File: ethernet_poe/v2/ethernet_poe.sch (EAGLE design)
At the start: 86 parts, among them J3 ARJM11C7-104-AB-EW2, Q1 BSR16, U1 AZ1117EH-3.3TRG1, U2 IFX91041, U3 W5500, U4 TPS26600PWPR, X1 25MHz

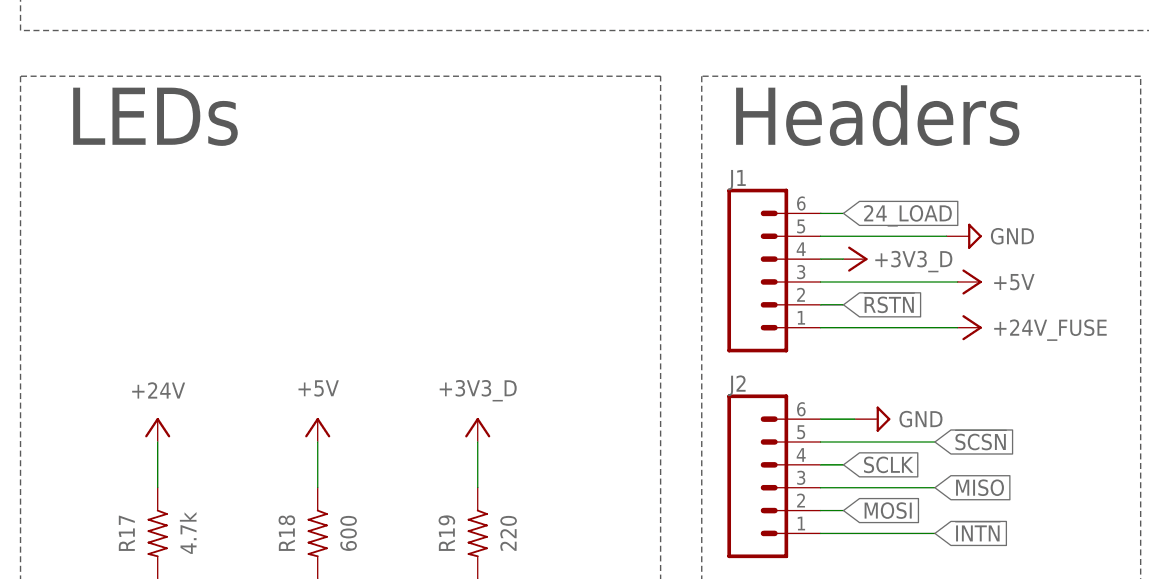
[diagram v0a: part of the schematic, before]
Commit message: routing for efuse
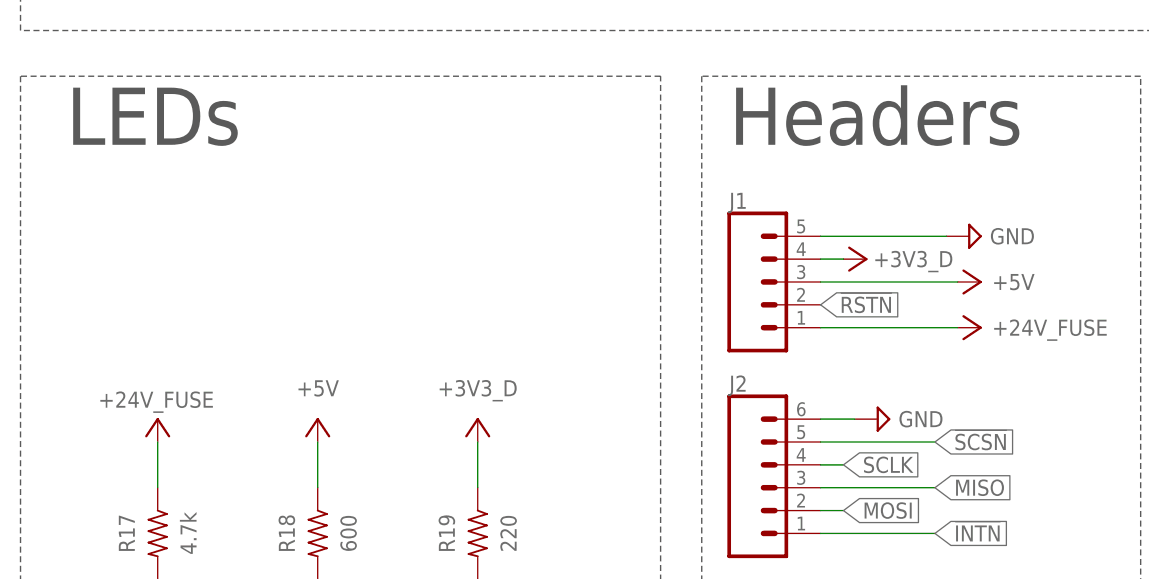
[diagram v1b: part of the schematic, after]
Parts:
- J1: device SparkFun-Connectors:CONN_06SILK_FEMALE_PTH -> SparkFun-Connectors:CONN_05
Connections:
- net +24V: no longer R17.1
- net +24V_FUSE: now also R17.1
- net 24_LOAD: no longer J1.6
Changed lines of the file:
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@@
 <?xml version="1.0" encoding="utf-8"?>
 <!DOCTYPE eagle SYSTEM "eagle.dtd">
-<eagle version="9.6.0">
+<eagle version="9.5.2">
 <drawing>
 <settings>
@@
 <part name="SUPPLY7" library="supply2" library_urn="urn:adsk.eagle:library:372" deviceset="GND" device=""/>
 <part name="C15" library="rcl" library_urn="urn:adsk.eagle:library:334" deviceset="CPOL-US" device="E2-5" package3d_urn="urn:adsk.eagle:package:23346/2" value="100uF"/>
-<part name="J1" library="SparkFun-Connectors" library_urn="urn:adsk.eagle:library:513" deviceset="CONN_06" device="SILK_FEMALE_PTH" package3d_urn="urn:adsk.eagle:package:38009/1"/>
+<part name="J1" library="SparkFun-Connectors" deviceset="CONN_05" device="" package3d_urn="urn:adsk.eagle:package:38104/1"/>
 <part name="J2" library="SparkFun-Connectors" library_urn="urn:adsk.eagle:library:513" deviceset="CONN_06" device="SILK_FEMALE_PTH" package3d_urn="urn:adsk.eagle:package:38009/1"/>
 <part name="SUPPLY12" library="supply2" library_urn="urn:adsk.eagle:library:372" deviceset="GND" device=""/>
@@
 <part name="+24V_FUSE2" library="ethernet_poe" deviceset="+24V_FUSE" device=""/>
 <part name="R30" library="rcl" library_urn="urn:adsk.eagle:library:334" deviceset="R-US_" device="R0603" package3d_urn="urn:adsk.eagle:package:23555/3" value="715k"/>
-<part name="+24V3" library="ethernet_poe" deviceset="+24V" device=""/>
 <part name="R31" library="rcl" library_urn="urn:adsk.eagle:library:334" deviceset="R-US_" device="R0603" package3d_urn="urn:adsk.eagle:package:23555/3" value="20k"/>
 <part name="R32" library="rcl" library_urn="urn:adsk.eagle:library:334" deviceset="R-US_" device="R0603" package3d_urn="urn:adsk.eagle:package:23555/3" value="30.1k"/>
@@
 <part name="SUPPLY30" library="supply2" library_urn="urn:adsk.eagle:library:372" deviceset="GND" device=""/>
 <part name="+24V_FUSE3" library="ethernet_poe" deviceset="+24V_FUSE" device=""/>
+<part name="+24V_FUSE4" library="ethernet_poe" deviceset="+24V_FUSE" device=""/>
 </parts>
 <sheets>
@@
 <attribute name="VALUE" x="313.436" y="216.789" size="1.778" layer="96"/>
 </instance>
-<instance part="J1" gate="G$1" x="91.44" y="119.38" smashed="yes">
-<attribute name="VALUE" x="88.9" y="109.474" size="1.778" layer="96" font="vector"/>
-<attribute name="NAME" x="86.36" y="130.048" size="1.778" layer="95"/>
+<instance part="J1" gate="G$1" x="88.9" y="119.38" smashed="yes">
+<attribute name="VALUE" x="86.36" y="109.474" size="1.778" layer="96" font="vector"/>
+<attribute name="NAME" x="86.36" y="127.508" size="1.778" layer="95"/>
 </instance>
 <instance part="J2" gate="G$1" x="91.44" y="96.52" smashed="yes">
@@
 <attribute name="VALUE" x="328.93" y="109.22" size="1.778" layer="96"/>
 </instance>
-<instance part="+24V3" gate="G$1" x="22.86" y="104.14" smashed="yes">
-<attribute name="VALUE" x="22.86" y="106.426" size="1.778" layer="96" align="bottom-center"/>
-</instance>
 <instance part="R31" gate="G$1" x="327.66" y="96.52" smashed="yes" rot="R270">
 <attribute name="NAME" x="328.93" y="96.52" size="1.778" layer="95"/>
@@
 <instance part="+24V_FUSE3" gate="G$1" x="218.44" y="254" smashed="yes">
 <attribute name="VALUE" x="211.836" y="255.27" size="1.778" layer="96"/>
+</instance>
+<instance part="+24V_FUSE4" gate="G$1" x="22.86" y="104.14" smashed="yes">
+<attribute name="VALUE" x="16.256" y="105.41" size="1.778" layer="96"/>
 </instance>
 </instances>
@@
 <segment>
 <pinref part="+3V3_D9" gate="G$1" pin="+3V3_D"/>
-<wire x1="99.06" y1="121.92" x2="96.52" y2="121.92" width="0.1524" layer="91"/>
 <pinref part="J1" gate="G$1" pin="4"/>
+<wire x1="96.52" y1="121.92" x2="99.06" y2="121.92" width="0.1524" layer="91"/>
 </segment>
 <segment>
@@
 </segment>
 <segment>
-<pinref part="R17" gate="G$1" pin="1"/>
-<wire x1="22.86" y1="96.52" x2="22.86" y2="101.6" width="0.1524" layer="91"/>
-<pinref part="+24V3" gate="G$1" pin="+24V"/>
-</segment>
-<segment>
 <pinref part="U4" gate="A" pin="!SHDN"/>
 <wire x1="393.7" y1="104.14" x2="406.4" y2="104.14" width="0.1524" layer="91"/>
@@
 </segment>
 <segment>
-<label x="99.06" y="116.84" size="1.778" layer="95" xref="yes"/>
-<wire x1="96.52" y1="116.84" x2="99.06" y2="116.84" width="0.1524" layer="91"/>
+<label x="96.52" y="116.84" size="1.778" layer="95" xref="yes"/>
 <pinref part="J1" gate="G$1" pin="2"/>
 </segment>
@@
 <pinref part="+24V_FUSE3" gate="G$1" pin="+24V_FUSE"/>
 </segment>
+<segment>
+<pinref part="R17" gate="G$1" pin="1"/>
+<wire x1="22.86" y1="96.52" x2="22.86" y2="101.6" width="0.1524" layer="91"/>
+<pinref part="+24V_FUSE4" gate="G$1" pin="+24V_FUSE"/>
+</segment>
 </net>
 <net name="N$9" class="0">
@@
 </segment>
 </net>
-<net name="N$33" class="0">
+<net name="N$33" class="1">
 <segment>
 <pinref part="U4" gate="A" pin="ILIM"/>
@@
 <label x="408.94" y="99.06" size="1.778" layer="95" xref="yes"/>
 </segment>
-<segment>
-<pinref part="J1" gate="G$1" pin="6"/>
-<wire x1="96.52" y1="127" x2="99.06" y2="127" width="0.1524" layer="91"/>
-<label x="99.06" y="127" size="1.778" layer="95" xref="yes"/>
-</segment>
-</net>
+</net>

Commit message: Pre Review Commit, Completed Routing
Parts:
- added H1, H2: MOUNT-PAD-ROUND2.8, holes:MOUNT-PAD-ROUND2.8
- J2: device SparkFun-Connectors:CONN_06SILK_FEMALE_PTH -> SparkFun-Connectors:CONN_07
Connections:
- net 24_LOAD: now also J2.7
- net GND: now also H1.MOUNT, H2.MOUNT
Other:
- note removed: "Add pi filter"
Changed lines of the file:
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@@
 <part name="C15" library="rcl" library_urn="urn:adsk.eagle:library:334" deviceset="CPOL-US" device="E2-5" package3d_urn="urn:adsk.eagle:package:23346/2" value="100uF"/>
 <part name="J1" library="SparkFun-Connectors" deviceset="CONN_05" device="" package3d_urn="urn:adsk.eagle:package:38104/1"/>
-<part name="J2" library="SparkFun-Connectors" library_urn="urn:adsk.eagle:library:513" deviceset="CONN_06" device="SILK_FEMALE_PTH" package3d_urn="urn:adsk.eagle:package:38009/1"/>
+<part name="J2" library="SparkFun-Connectors" library_urn="urn:adsk.eagle:library:513" deviceset="CONN_07" device="" package3d_urn="urn:adsk.eagle:package:38129/1"/>
 <part name="SUPPLY12" library="supply2" library_urn="urn:adsk.eagle:library:372" deviceset="GND" device=""/>
 <part name="P+7" library="supply1" library_urn="urn:adsk.eagle:library:371" deviceset="+5V" device=""/>
@@
 <part name="+24V_FUSE3" library="ethernet_poe" deviceset="+24V_FUSE" device=""/>
 <part name="+24V_FUSE4" library="ethernet_poe" deviceset="+24V_FUSE" device=""/>
+<part name="SUPPLY31" library="supply2" library_urn="urn:adsk.eagle:library:372" deviceset="GND" device=""/>
+<part name="H1" library="holes" library_urn="urn:adsk.eagle:library:237" deviceset="MOUNT-PAD-ROUND" device="2.8" package3d_urn="urn:adsk.eagle:package:14281/1"/>
+<part name="H2" library="holes" library_urn="urn:adsk.eagle:library:237" deviceset="MOUNT-PAD-ROUND" device="2.8" package3d_urn="urn:adsk.eagle:package:14281/1"/>
+<part name="SUPPLY32" library="supply2" library_urn="urn:adsk.eagle:library:372" deviceset="GND" device=""/>
 </parts>
 <sheets>
@@
 blown-fuse-indicator-circuit-
 using-one-transistor/</text>
-<text x="223.52" y="241.3" size="1.778" layer="91">Add pi filter</text>
 <text x="335.28" y="157.48" size="1.778" layer="97">NOTE: This pi filter isolates the digital
 and analog 3.3V power supplies by
@@
 <attribute name="NAME" x="86.36" y="127.508" size="1.778" layer="95"/>
 </instance>
-<instance part="J2" gate="G$1" x="91.44" y="96.52" smashed="yes">
-<attribute name="VALUE" x="88.9" y="86.614" size="1.778" layer="96" font="vector"/>
-<attribute name="NAME" x="86.36" y="107.188" size="1.778" layer="95"/>
+<instance part="J2" gate="G$1" x="91.44" y="91.44" smashed="yes">
+<attribute name="VALUE" x="88.9" y="81.534" size="1.778" layer="96" font="vector"/>
+<attribute name="NAME" x="86.36" y="104.648" size="1.778" layer="95"/>
 </instance>
 <instance part="SUPPLY12" gate="GND" x="113.03" y="124.46" smashed="yes" rot="R90">
@@
 <attribute name="VALUE" x="415.036" y="112.649" size="1.778" layer="96"/>
 </instance>
-<instance part="SUPPLY30" gate="GND" x="102.87" y="104.14" smashed="yes" rot="R90">
-<attribute name="VALUE" x="105.156" y="104.14" size="1.778" layer="96" align="center-left"/>
+<instance part="SUPPLY30" gate="GND" x="102.87" y="99.06" smashed="yes" rot="R90">
+<attribute name="VALUE" x="105.156" y="99.06" size="1.778" layer="96" align="center-left"/>
 </instance>
 <instance part="+24V_FUSE3" gate="G$1" x="218.44" y="254" smashed="yes">
@@
 <instance part="+24V_FUSE4" gate="G$1" x="22.86" y="104.14" smashed="yes">
 <attribute name="VALUE" x="16.256" y="105.41" size="1.778" layer="96"/>
+</instance>
+<instance part="SUPPLY31" gate="GND" x="40.64" y="7.62" smashed="yes">
+<attribute name="VALUE" x="40.64" y="5.588" size="1.778" layer="96" align="top-center"/>
+</instance>
+<instance part="H1" gate="G$1" x="48.26" y="12.7" smashed="yes">
+<attribute name="NAME" x="51.054" y="13.2842" size="1.778" layer="95"/>
+<attribute name="VALUE" x="42.418" y="7.9502" size="1.778" layer="96"/>
+</instance>
+<instance part="H2" gate="G$1" x="81.28" y="12.7" smashed="yes">
+<attribute name="NAME" x="84.074" y="13.2842" size="1.778" layer="95"/>
+<attribute name="VALUE" x="75.946" y="7.9502" size="1.778" layer="96"/>
+</instance>
+<instance part="SUPPLY32" gate="GND" x="73.66" y="7.62" smashed="yes">
+<attribute name="VALUE" x="73.66" y="5.588" size="1.778" layer="96" align="top-center"/>
 </instance>
 </instances>
@@
 <segment>
 <pinref part="J2" gate="G$1" pin="6"/>
-<wire x1="96.52" y1="104.14" x2="100.33" y2="104.14" width="0.1524" layer="91"/>
+<wire x1="96.52" y1="99.06" x2="100.33" y2="99.06" width="0.1524" layer="91"/>
 <pinref part="SUPPLY30" gate="GND" pin="GND"/>
+</segment>
+<segment>
+<pinref part="SUPPLY31" gate="GND" pin="GND"/>
+<wire x1="40.64" y1="10.16" x2="40.64" y2="12.7" width="0.1524" layer="91"/>
+<pinref part="H1" gate="G$1" pin="MOUNT"/>
+<wire x1="40.64" y1="12.7" x2="45.72" y2="12.7" width="0.1524" layer="91"/>
+</segment>
+<segment>
+<pinref part="SUPPLY32" gate="GND" pin="GND"/>
+<wire x1="73.66" y1="10.16" x2="73.66" y2="12.7" width="0.1524" layer="91"/>
+<pinref part="H2" gate="G$1" pin="MOUNT"/>
+<wire x1="73.66" y1="12.7" x2="78.74" y2="12.7" width="0.1524" layer="91"/>
 </segment>
 </net>
@@
 </segment>
 <segment>
-<label x="109.22" y="101.6" size="1.778" layer="95" xref="yes"/>
-<wire x1="96.52" y1="101.6" x2="109.22" y2="101.6" width="0.1524" layer="91"/>
+<label x="109.22" y="96.52" size="1.778" layer="95" xref="yes"/>
+<wire x1="96.52" y1="96.52" x2="109.22" y2="96.52" width="0.1524" layer="91"/>
 <pinref part="J2" gate="G$1" pin="5"/>
 </segment>
@@
 </segment>
 <segment>
-<wire x1="96.52" y1="99.06" x2="99.06" y2="99.06" width="0.1524" layer="91"/>
-<label x="99.06" y="99.06" size="1.778" layer="95" xref="yes"/>
+<wire x1="96.52" y1="93.98" x2="99.06" y2="93.98" width="0.1524" layer="91"/>
+<label x="99.06" y="93.98" size="1.778" layer="95" xref="yes"/>
 <pinref part="J2" gate="G$1" pin="4"/>
 </segment>
@@
 </segment>
 <segment>
-<wire x1="96.52" y1="96.52" x2="109.22" y2="96.52" width="0.1524" layer="91"/>
-<label x="109.22" y="96.52" size="1.778" layer="95" xref="yes"/>
+<wire x1="96.52" y1="91.44" x2="109.22" y2="91.44" width="0.1524" layer="91"/>
+<label x="109.22" y="91.44" size="1.778" layer="95" xref="yes"/>
 <pinref part="J2" gate="G$1" pin="3"/>
 </segment>
@@
 </segment>
 <segment>
-<wire x1="96.52" y1="93.98" x2="99.06" y2="93.98" width="0.1524" layer="91"/>
-<label x="99.06" y="93.98" size="1.778" layer="95" xref="yes"/>
+<wire x1="96.52" y1="88.9" x2="99.06" y2="88.9" width="0.1524" layer="91"/>
+<label x="99.06" y="88.9" size="1.778" layer="95" xref="yes"/>
 <pinref part="J2" gate="G$1" pin="2"/>
 </segment>
@@
 </segment>
 <segment>
-<label x="109.22" y="91.44" size="1.778" layer="95" xref="yes"/>
-<wire x1="96.52" y1="91.44" x2="109.22" y2="91.44" width="0.1524" layer="91"/>
+<label x="109.22" y="86.36" size="1.778" layer="95" xref="yes"/>
+<wire x1="96.52" y1="86.36" x2="109.22" y2="86.36" width="0.1524" layer="91"/>
 <pinref part="J2" gate="G$1" pin="1"/>
 </segment>
@@
 </segment>
 <segment>
-<label x="96.52" y="116.84" size="1.778" layer="95" xref="yes"/>
+<label x="101.6" y="116.84" size="1.778" layer="95" xref="yes"/>
 <pinref part="J1" gate="G$1" pin="2"/>
+<wire x1="96.52" y1="116.84" x2="101.6" y2="116.84" width="0.1524" layer="91"/>
 </segment>
 <segment>
@@
 <label x="408.94" y="99.06" size="1.778" layer="95" xref="yes"/>
 </segment>
-</net>
+<segment>
+<pinref part="J2" gate="G$1" pin="7"/>
+<wire x1="96.52" y1="101.6" x2="109.22" y2="101.6" width="0.1524" layer="91"/>
+<label x="109.22" y="101.6" size="1.778" layer="95" xref="yes"/>
+</segment>
+</net>

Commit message: Additional design review updates
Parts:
- C1: value 22nF -> 22nF, 50V
- C27, C28: value (none) -> TBD
- C3: value 2.2uF -> 2.2uF, 50V
- C30: value 1uF -> 1uF, 50V
- C31: value 2.2mF -> 2.2mF, 50V
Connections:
- new net !RST: C17.1, R20.1, S1.2
- net !RSTN: no longer C17.1, R20.1, S1.2
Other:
- note added: "3.3V Analog"
- note added: "Filtering"
- note added: "GND Analog"
- note added: "Mounting Holes"
- note added: "NOTE: This pi filter isolates the digital and analog 3.3V power supplies by attenuating differential mode noise. Cap values TBD based on noise."
- note added: "Power (24V-5V)"
- note added: "Power (5V-3.3V)"
- note removed: "3.3V Analog Filtering"
- note removed: "NOTE: This pi filter isolates the digital and analog 3.3V power supplies by attenuating differential mode noise."
- note removed: "Power"
- moved on the sheet: C1, C10, C11, C12, C13, C14, C15, C16, C17, C18, C19, C2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

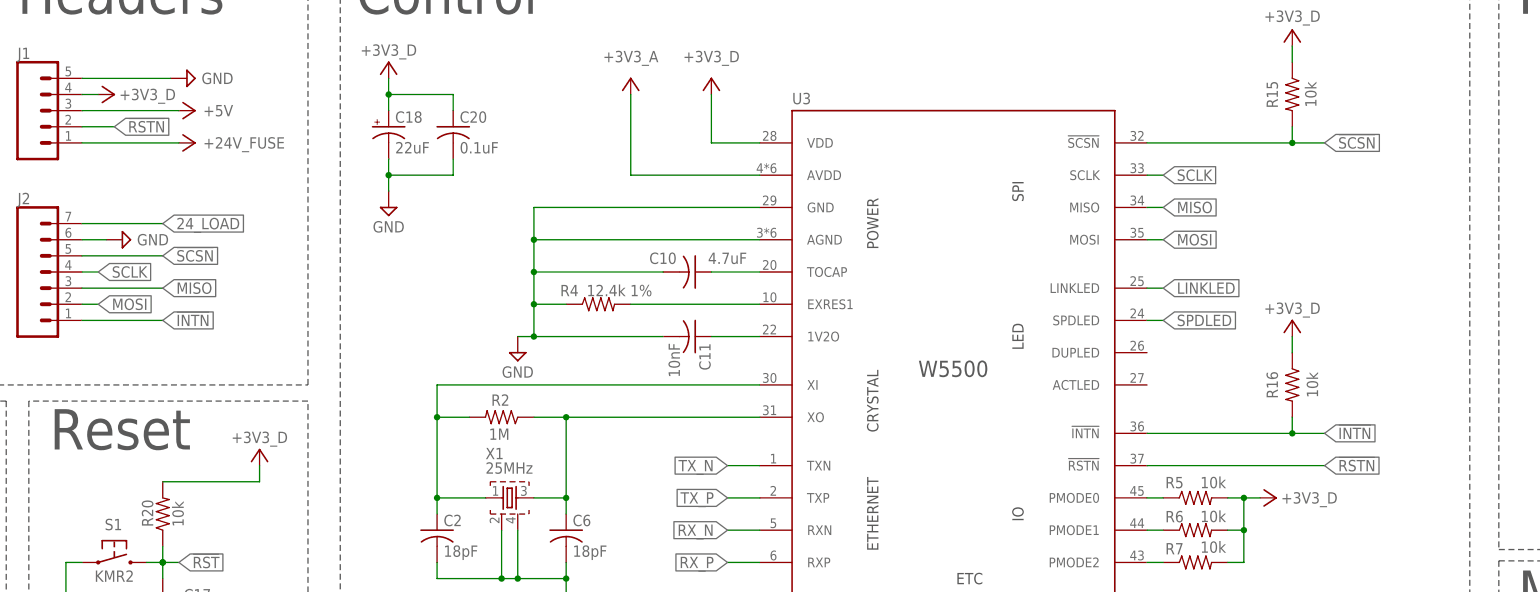
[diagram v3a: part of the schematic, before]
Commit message: Made drc compliant
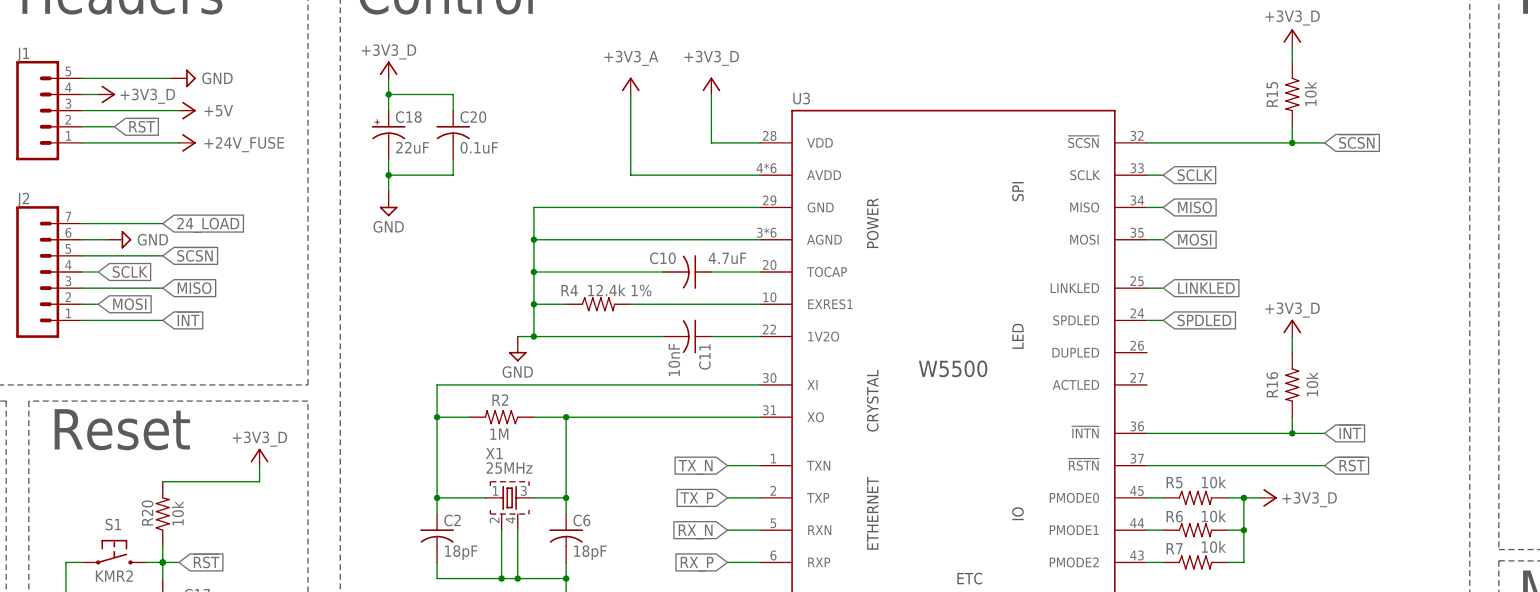
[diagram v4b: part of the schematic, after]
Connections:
- net !INTN renamed !INT
- removed net !RSTN: J1.2, U3.!RSTN
- net !RST: now also J1.2, U3.!RSTN
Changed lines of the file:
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@@
-</segment>
-</net>
-<net name="!INTN" class="0">
-<segment>
-<pinref part="U3" gate="G$1" pin="!INTN"/>
-<wire x1="264.16" y1="96.52" x2="287.02" y2="96.52" width="0.1524" layer="91"/>
-<label x="292.1" y="96.52" size="1.778" layer="95" xref="yes"/>
-<pinref part="R16" gate="G$1" pin="2"/>
-<wire x1="287.02" y1="96.52" x2="292.1" y2="96.52" width="0.1524" layer="91"/>
-<wire x1="287.02" y1="99.06" x2="287.02" y2="96.52" width="0.1524" layer="91"/>
-<junction x="287.02" y="96.52"/>
-</segment>
-<segment>
-<label x="109.22" y="114.3" size="1.778" layer="95" xref="yes"/>
-<wire x1="96.52" y1="114.3" x2="109.22" y2="114.3" width="0.1524" layer="91"/>
-<pinref part="J2" gate="G$1" pin="1"/>
-</segment>
-</net>
-<net name="!RSTN" class="0">
-<segment>
-<pinref part="U3" gate="G$1" pin="!RSTN"/>
-<wire x1="264.16" y1="91.44" x2="292.1" y2="91.44" width="0.1524" layer="91"/>
-<label x="292.1" y="91.44" size="1.778" layer="95" xref="yes"/>
-</segment>
-<segment>
-<label x="101.6" y="144.78" size="1.778" layer="95" xref="yes"/>
-<pinref part="J1" gate="G$1" pin="2"/>
-<wire x1="96.52" y1="144.78" x2="101.6" y2="144.78" width="0.1524" layer="91"/>
 </segment>
 </net>
@@
 <wire x1="109.22" y1="76.2" x2="109.22" y2="78.74" width="0.1524" layer="91"/>
 </segment>
-</net>
+<segment>
+<pinref part="U3" gate="G$1" pin="!RSTN"/>
+<wire x1="264.16" y1="91.44" x2="292.1" y2="91.44" width="0.1524" layer="91"/>
+<label x="292.1" y="91.44" size="1.778" layer="95" xref="yes"/>
+</segment>
+<segment>
+<label x="101.6" y="144.78" size="1.778" layer="95" xref="yes"/>
+<pinref part="J1" gate="G$1" pin="2"/>
+<wire x1="96.52" y1="144.78" x2="101.6" y2="144.78" width="0.1524" layer="91"/>
+</segment>
+</net>
+<net name="!INT" class="0">
+<segment>
+<pinref part="U3" gate="G$1" pin="!INTN"/>
+<wire x1="264.16" y1="96.52" x2="287.02" y2="96.52" width="0.1524" layer="91"/>
+<label x="292.1" y="96.52" size="1.778" layer="95" xref="yes"/>
+<pinref part="R16" gate="G$1" pin="2"/>
+<wire x1="287.02" y1="96.52" x2="292.1" y2="96.52" width="0.1524" layer="91"/>
+<wire x1="287.02" y1="99.06" x2="287.02" y2="96.52" width="0.1524" layer="91"/>
+<junction x="287.02" y="96.52"/>
+</segment>
+<segment>
+<label x="109.22" y="114.3" size="1.778" layer="95" xref="yes"/>
+<wire x1="96.52" y1="114.3" x2="109.22" y2="114.3" width="0.1524" layer="91"/>
+<pinref part="J2" gate="G$1" pin="1"/>
+</segment>
+</net>
